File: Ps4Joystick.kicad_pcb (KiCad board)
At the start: 2 copper layers, 34 x 26 mm, 3 parts, among them J1 Conn_01x05

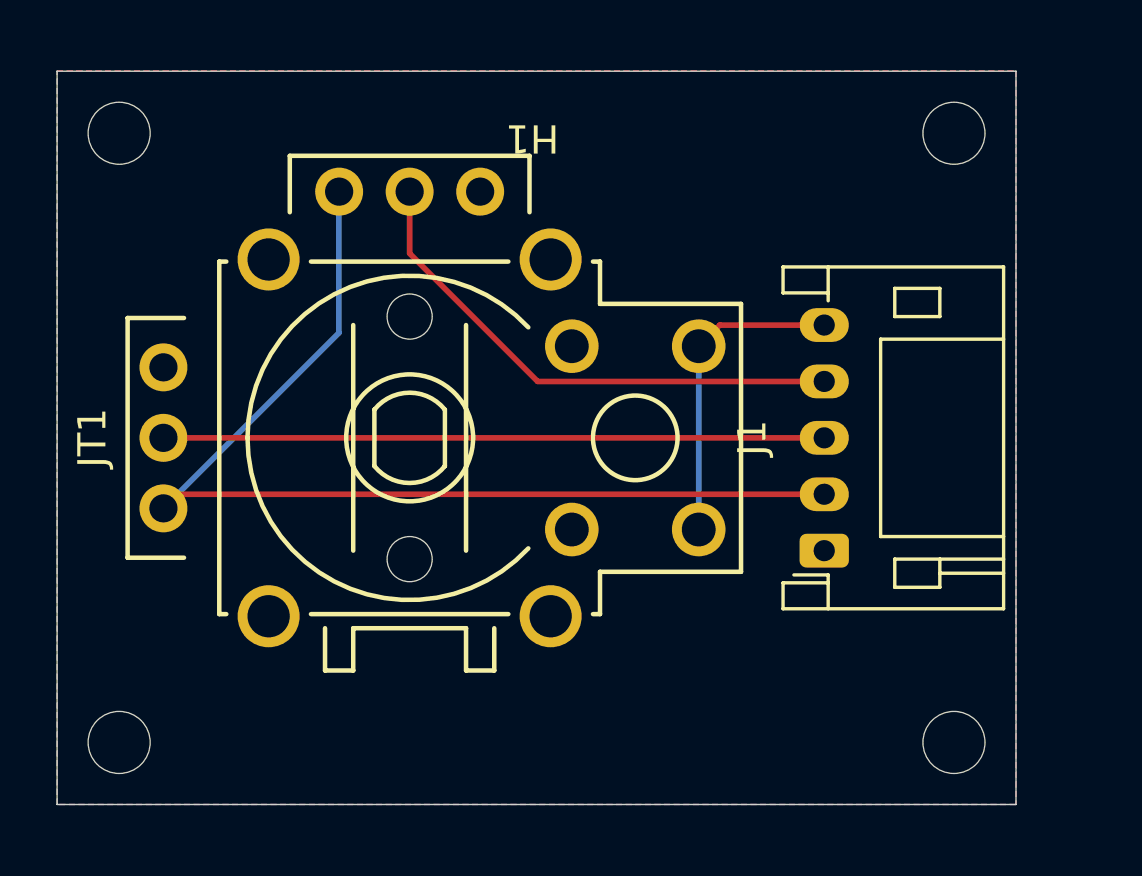
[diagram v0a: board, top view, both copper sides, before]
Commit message: increase joystick board size
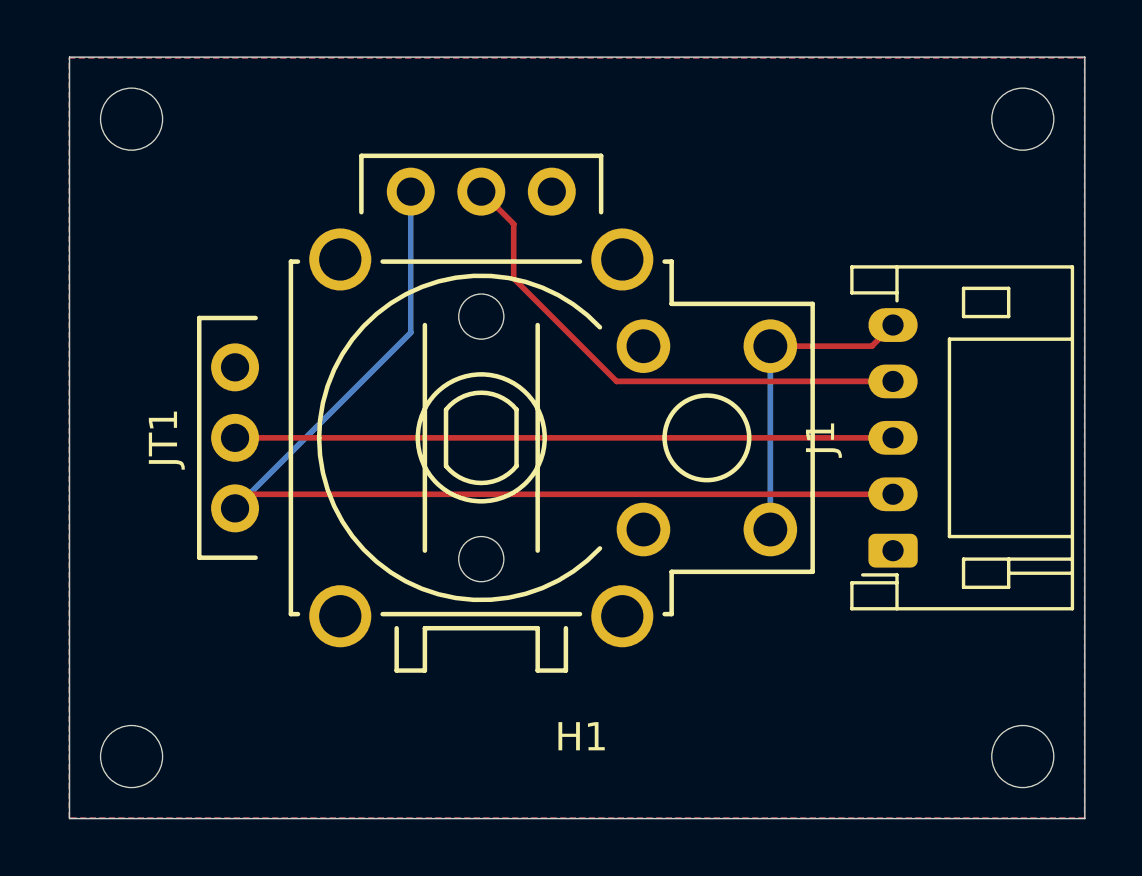
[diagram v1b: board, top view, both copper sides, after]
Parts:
- moved JT1 2.54 mm to (-3.40, 0.00)
- moved J1 2.44 mm to (11.2, 4.00)
- moved H1 1.44 mm to (0.00, 0.00), turned to 0 degrees
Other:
- board size 34 x 26 mm -> 36 x 27 mm
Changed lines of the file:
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@@
 	(footprint "ErgoCai.pretty:Ps4JoystickMount"
 		(layer "F.Cu")
-		(at -1.44 0 180)
+		(at 0 0)
 		(property "Reference" "H1"
-			(at 0.1524 10.6172 180)
+			(at 0.1524 10.6172 0)
 			(unlocked yes)
 			(layer "F.SilkS")
@@
 		)
 		(property "Value" "MountingHole"
-			(at -0.0254 12.1158 180)
+			(at -0.0254 12.1158 0)
 			(unlocked yes)
 			(layer "F.Fab")
@@
 		)
 		(property "Datasheet" "~"
-			(at 0 0 180)
+			(at 0 0 0)
 			(unlocked yes)
 			(layer "F.Fab")
@@
 		)
 		(property "Description" "Mounting Hole without connection"
-			(at 0 0 180)
+			(at 0 0 0)
 			(unlocked yes)
 			(layer "F.Fab")
@@
 		(attr exclude_from_pos_files exclude_from_bom)
 		(fp_line
-			(start 17 -13)
-			(end 17 13)
+			(start -18 -13.5)
+			(end -18 13.5)
 			(stroke
 				(width 0.1)
@@
 		)
 		(fp_line
-			(start -17 13)
-			(end 17 13)
+			(start -18 -13.5)
+			(end 18 -13.5)
 			(stroke
 				(width 0.1)
@@
 		)
 		(fp_line
-			(start -17 -13)
-			(end 17 -13)
+			(start -18 13.5)
+			(end 18 13.5)
 			(stroke
 				(width 0.1)
@@
 		)
 		(fp_line
-			(start -17 -13)
-			(end -17 13)
+			(start 18 -13.5)
+			(end 18 13.5)
 			(stroke
 				(width 0.1)
@@
 		)
 		(fp_circle
-			(center 14.8 10.8)
-			(end 16.7 10.8)
+			(center -15.8 -11.3)
+			(end -13.9 -11.3)
 			(stroke
 				(width 0.15)
@@
 		)
 		(fp_circle
-			(center 14.8 -10.8)
-			(end 16.7 -10.8)
+			(center -15.8 11.3)
+			(end -13.9 11.3)
 			(stroke
 				(width 0.15)
@@
 		)
 		(fp_circle
-			(center -14.8 10.8)
-			(end -12.9 10.8)
+			(center 15.8 -11.3)
+			(end 17.7 -11.3)
 			(stroke
 				(width 0.15)
@@
 		)
 		(fp_circle
-			(center -14.8 -10.8)
-			(end -12.9 -10.8)
+			(center 15.8 11.3)
+			(end 17.7 11.3)
 			(stroke
 				(width 0.15)
@@
 		)
 		(fp_circle
-			(center 14.8 10.8)
-			(end 16.95 10.8)
+			(center -15.8 -11.3)
+			(end -13.65 -11.3)
 			(stroke
 				(width 0.05)
@@
 		)
 		(fp_circle
-			(center 14.8 -10.8)
-			(end 16.95 -10.8)
+			(center -15.8 11.3)
+			(end -13.65 11.3)
 			(stroke
 				(width 0.05)
@@
 		)
 		(fp_circle
-			(center -14.8 10.8)
-			(end -12.65 10.8)
+			(center 15.8 -11.3)
+			(end 17.95 -11.3)
 			(stroke
 				(width 0.05)
@@
 		)
 		(fp_circle
-			(center -14.8 -10.8)
-			(end -12.65 -10.8)
+			(center 15.8 11.3)
+			(end 17.95 11.3)
 			(stroke
 				(width 0.05)
@@
 		)
 		(pad "" np_thru_hole circle
-			(at -14.8 -10.8 180)
+			(at -15.8 -11.3)
 			(size 2.2 2.2)
 			(drill 2.2)
@@
 		)
 		(pad "" np_thru_hole circle
-			(at -14.8 10.8 180)
+			(at -15.8 11.3)
 			(size 2.2 2.2)
 			(drill 2.2)
@@
 		)
 		(pad "" np_thru_hole circle
-			(at 14.8 -10.8 180)
+			(at 15.8 -11.3)
 			(size 2.2 2.2)
 			(drill 2.2)
@@
 		)
 		(pad "" np_thru_hole circle
-			(at 14.8 10.8 180)
+			(at 15.8 11.3)
 			(size 2.2 2.2)
 			(drill 2.2)
@@
 	(footprint "ErgoCai.pretty:Alpsalpine_RKJXV122400R"
 		(layer "F.Cu")
-		(at -5.94 0 90)
+		(at -3.4 0 90)
 		(property "Reference" "JT1"
 			(at 0 -11.25 90)
@@
 			(polygon
 				(pts
-					(xy -8.94 -2.5) (xy -9.94 -2.5) (xy -10.44 -3) (xy -10.44 -4) (xy -9.94 -4.5) (xy -8.94 -4.5) (xy -8.44 -4)
-					(xy -8.44 -3)
+					(xy -6.4 -2.5) (xy -7.4 -2.5) (xy -7.9 -3) (xy -7.9 -4) (xy -7.4 -4.5) (xy -6.4 -4.5) (xy -5.9 -4)
+					(xy -5.9 -3)
 				)
 			)
@@
 			(polygon
 				(pts
-					(xy -8.94 4.5) (xy -9.94 4.5) (xy -10.44 4) (xy -10.44 3) (xy -9.94 2.5) (xy -8.94 2.5) (xy -8.44 3)
-					(xy -8.44 4)
+					(xy -6.4 4.5) (xy -7.4 4.5) (xy -7.9 4) (xy -7.9 3) (xy -7.4 2.5) (xy -6.4 2.5) (xy -5.9 3) (xy -5.9 4)
 				)
 			)
@@
 			(polygon
 				(pts
-					(xy -1.94 -2.5) (xy -2.94 -2.5) (xy -3.44 -3) (xy -3.44 -4) (xy -2.94 -4.5) (xy -1.94 -4.5) (xy -1.44 -4)
-					(xy -1.44 -3)
+					(xy 0.6 -2.5) (xy -0.4 -2.5) (xy -0.9 -3) (xy -0.9 -4) (xy -0.4 -4.5) (xy 0.6 -4.5) (xy 1.1 -4)
+					(xy 1.1 -3)
 				)
 			)
@@
 			(polygon
 				(pts
-					(xy -1.94 4.5) (xy -2.94 4.5) (xy -3.44 4) (xy -3.44 3) (xy -2.94 2.5) (xy -1.94 2.5) (xy -1.44 3)
-					(xy -1.44 4)
+					(xy 0.6 4.5) (xy -0.4 4.5) (xy -0.9 4) (xy -0.9 3) (xy -0.4 2.5) (xy 0.6 2.5) (xy 1.1 3) (xy 1.1 4)
 				)
 			)
@@
 			(polygon
 				(pts
-					(xy 2.56 1.5) (xy -6.44 1.5) (xy -7.44 0.5) (xy -7.44 -0.5) (xy -6.44 -1.5) (xy 2.56 -1.5) (xy 3.56 -0.5)
-					(xy 3.56 0.5)
+					(xy 5.1 1.5) (xy -3.9 1.5) (xy -4.9 0.5) (xy -4.9 -0.5) (xy -3.9 -1.5) (xy 5.1 -1.5) (xy 6.1 -0.5)
+					(xy 6.1 0.5)
 				)
 			)
@@
 	(footprint "Connector_JST:JST_PH_S5B-PH-K_1x05_P2.00mm_Horizontal"
 		(layer "F.Cu")
-		(at 8.76 4 90)
+		(at 11.2 4 90)
 		(descr "JST PH series connector, S5B-PH-K (http://www.jst-mfg.com/product/pdf/eng/ePH.pdf), generated with kicad-footprint-generator")
 		(tags "connector JST PH horizontal")
@@
 	)
 	(gr_line
-		(start 15.56 -13)
-		(end -18.44 -13)
+		(start 18 -13.5)
+		(end -18 -13.5)
 		(stroke
 			(width 0.05)
@@
 	)
 	(gr_line
-		(start 15.56 13)
-		(end 15.56 -13)
+		(start 18 13.5)
+		(end 18 -13.5)
 		(stroke
 			(width 0.05)
@@
 	)
 	(gr_line
-		(start -18.44 -13)
-		(end -18.44 13)
+		(start -18 -13.5)
+		(end -18 13.5)
 		(stroke
 			(width 0.05)
@@
 	)
 	(gr_line
-		(start -18.44 13)
-		(end 15.56 13)
+		(start -18 13.5)
+		(end 18 13.5)
 		(stroke
 			(width 0.05)
@@
 	)
 	(segment
-		(start 8.72 -4)
-		(end 5.06 -4)
+		(start 6.85 -3.25)
+		(end 10.45 -3.25)
 		(width 0.2)
 		(layer "F.Cu")
@@
 	)
 	(segment
-		(start 5.06 -4)
-		(end 4.31 -3.25)
+		(start 10.45 -3.25)
+		(end 11.2 -4)
 		(width 0.2)
 		(layer "F.Cu")
@@
 	)
 	(segment
-		(start 4.31 3.25)
-		(end 4.31 -3.25)
+		(start 6.85 -3.25)
+		(end 6.85 3.25)
 		(width 0.2)
 		(layer "B.Cu")
@@
 	)
 	(segment
-		(start 8.72 2)
-		(end -14.17 2)
+		(start -11.63 2)
+		(end 11.2 2)
 		(width 0.2)
 		(layer "F.Cu")
@@
 	)
 	(segment
-		(start -14.17 2)
-		(end -14.67 2.5)
+		(start -12.13 2.5)
+		(end -11.63 2)
 		(width 0.2)
 		(layer "F.Cu")
@@
 	)
 	(segment
-		(start -8.45 -8.72)
-		(end -8.44 -8.73)
+		(start -12.13 2.5)
+		(end -5.9 -3.73)
 		(width 0.2)
 		(layer "B.Cu")
@@
 	)
 	(segment
-		(start -8.45 -3.72)
-		(end -8.45 -8.72)
+		(start -5.9 -3.73)
+		(end -5.9 -8.73)
 		(width 0.2)
 		(layer "B.Cu")
@@
 	)
 	(segment
-		(start -14.67 2.5)
-		(end -8.45 -3.72)
-		(width 0.2)
-		(layer "B.Cu")
-		(net 3)
-	)
-	(segment
-		(start 8.72 0)
-		(end -14.67 0)
+		(start -12.13 0)
+		(end 11.2 0)
 		(width 0.2)
 		(layer "F.Cu")
@@
 	)
 	(segment
-		(start -1.4 -2)
-		(end -5.94 -6.54)
+		(start 11.2 -2)
+		(end 1.4 -2)
 		(width 0.2)
 		(layer "F.Cu")
@@
 	)
 	(segment
-		(start 8.72 -2)
-		(end -1.4 -2)
+		(start -2.249 -5.649)
+		(end -2.249 -7.579)
 		(width 0.2)
 		(layer "F.Cu")
@@
 	)
 	(segment
-		(start -5.94 -6.54)
-		(end -5.94 -8.73)
+		(start 1.4 -2)
+		(end -2.249 -5.649)
+		(width 0.2)
+		(layer "F.Cu")
+		(net 5)
+	)
+	(segment
+		(start -2.249 -7.579)
+		(end -3.4 -8.73)
 		(width 0.2)
 		(layer "F.Cu")
@@
 		(polygon
 			(pts
-				(xy 15.55 13) (xy -18.44 13) (xy -18.44 -13.019868) (xy 15.56 -13.009868) (xy 15.56 13)
-			)
-		)
+				(xy -18.01 -13.47) (xy 17.99 -13.47) (xy 17.99 13.48) (xy -18.01 13.48)
+			)
+		)
